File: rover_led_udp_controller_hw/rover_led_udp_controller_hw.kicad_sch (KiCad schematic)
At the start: 0 parts

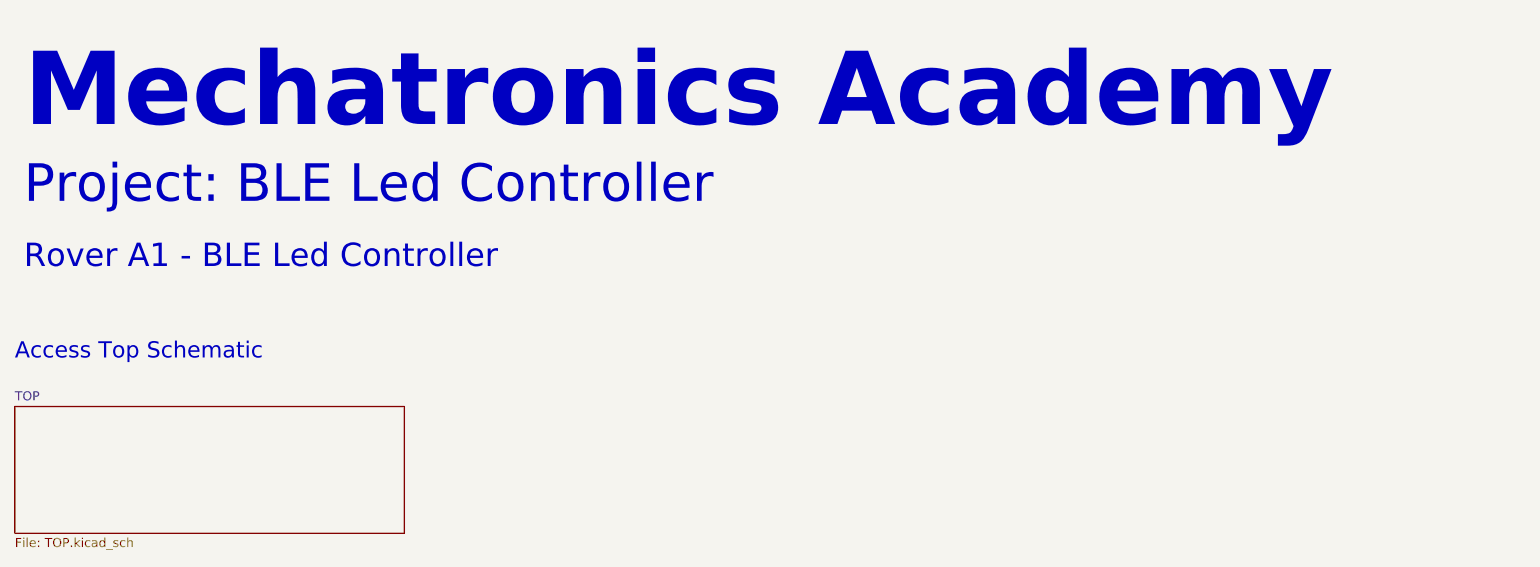
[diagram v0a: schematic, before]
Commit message: Rename project
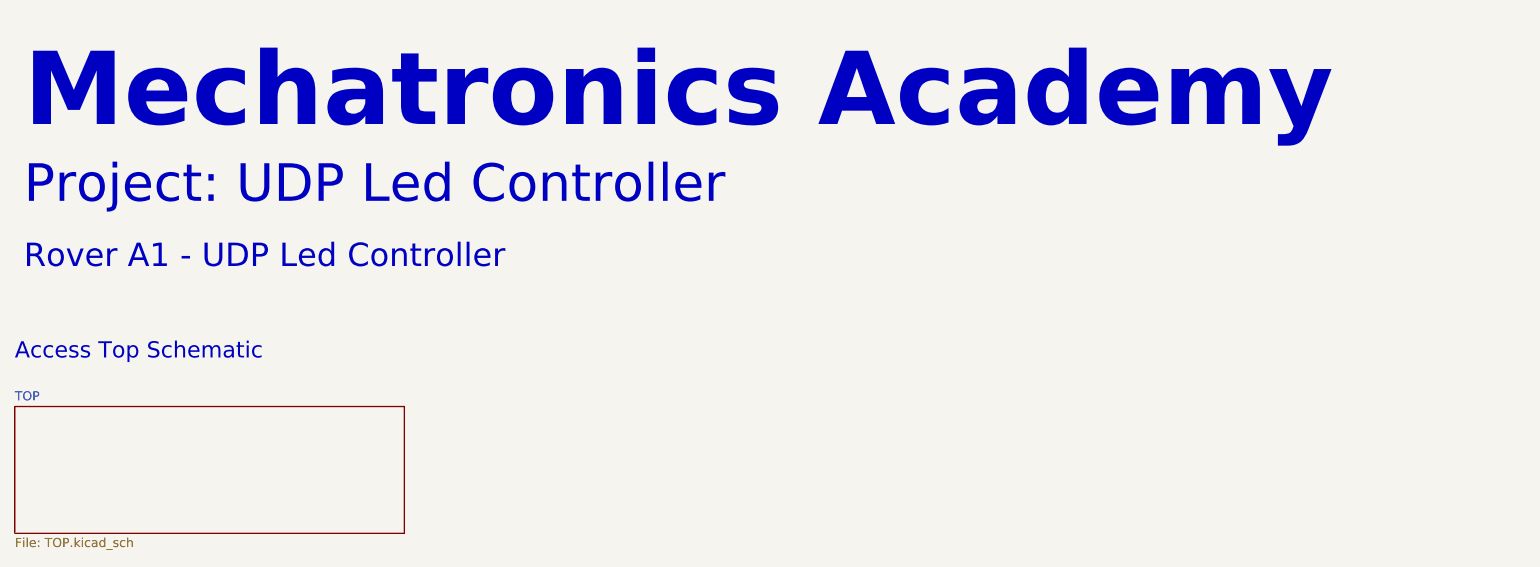
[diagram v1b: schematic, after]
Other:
- note added: "Project: UDP Led Controller"
- note added: "Rover A1 - UDP Led Controller"
- note removed: "Project: BLE Led Controller"
- note removed: "Rover A1 - BLE Led Controller"
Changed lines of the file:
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@@
 		(rev "1.0")
 	)
-	(text "Rover A1 - BLE Led Controller"
+	(text "Rover A1 - UDP Led Controller"
 		(exclude_from_sim no)
 		(at 71.12 66.04 0)
@@
 		)
 	)
-	(text "Project: BLE Led Controller"
+	(text "Project: UDP Led Controller"
 		(exclude_from_sim no)
 		(at 71.12 57.15 0)
@@
 				)
 			)
-			(project "rover_bms_ble_controller_hw"
+			(project "rover_led_udp_controller_hw"
 				(path "/a123a8db-a151-4387-aa00-5e9926b56231"
 					(page "2")
